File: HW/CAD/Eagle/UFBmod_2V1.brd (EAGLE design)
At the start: 98.4 x 89.5 mm, 197 parts, among them T0551 MMBT2222, U0501 MIDAS_MCCOG21605B6W-FPTLWI, U0601 MAX5217, U0701 AT86RF215-ZU, U0711 ASVTX-13-D-26.000MHZ-I05-T, U0811 PE4259, U0821 RFX1010, U0881 B39871B3440U410, U0911 FT232HL, U1101 TPS53353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

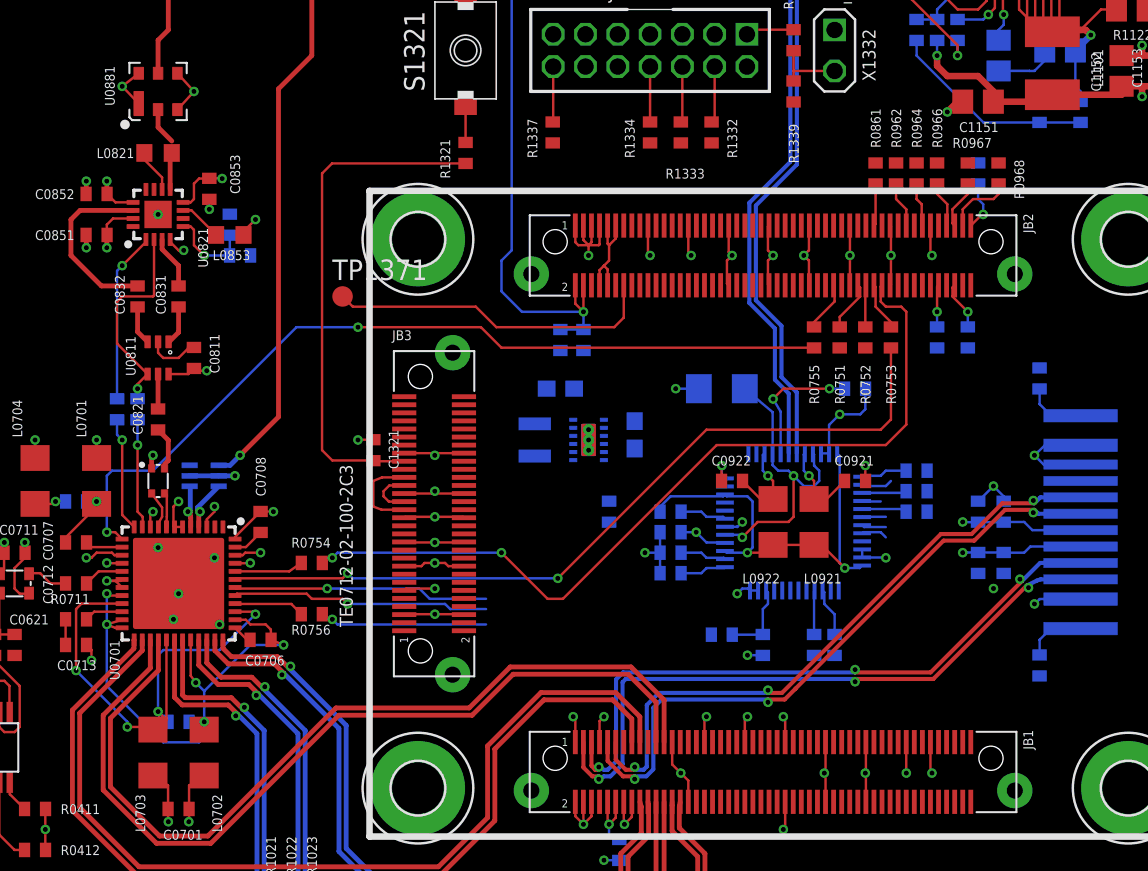
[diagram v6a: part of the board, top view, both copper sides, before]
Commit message: HW_2V0 - CAD/Eagle - some more wires routed
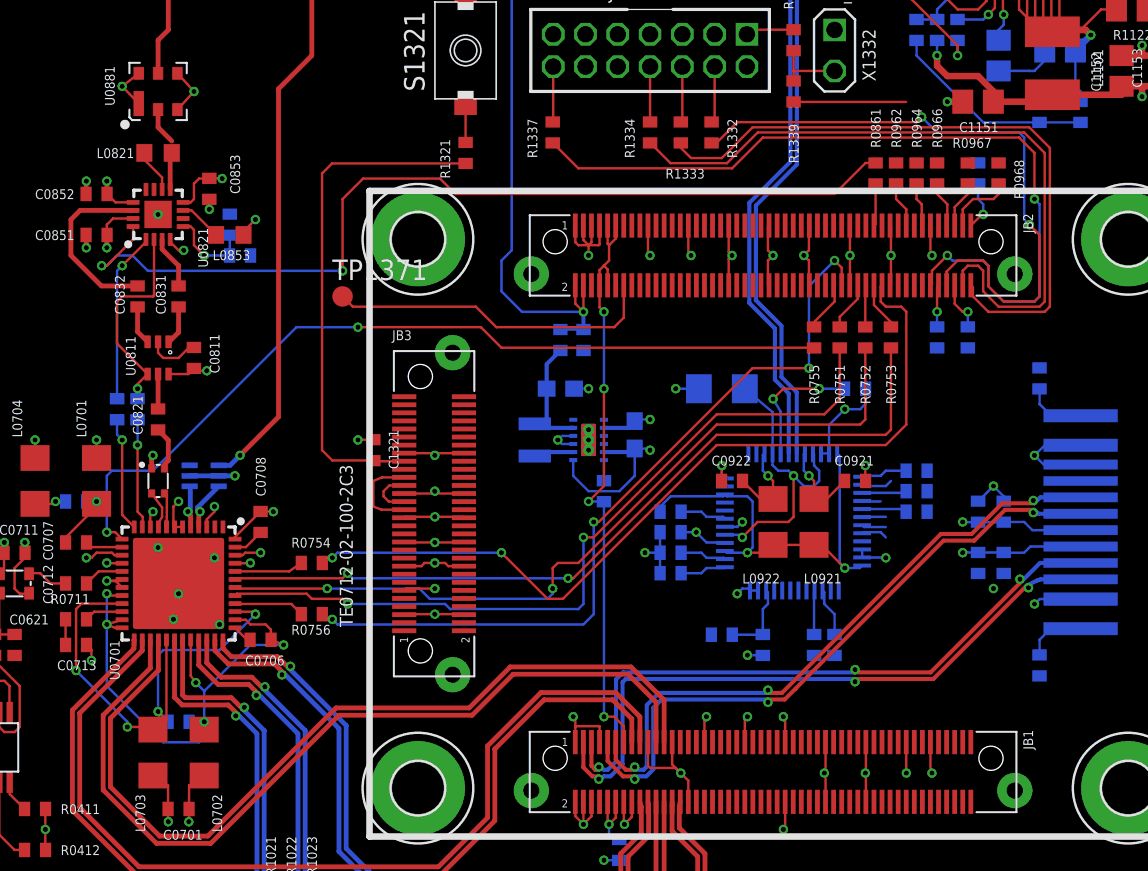
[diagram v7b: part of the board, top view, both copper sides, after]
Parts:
- moved R1211 1.31 mm to (45.4, 46.4)
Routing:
- net RFX_MODE: track 0.00 -> 58.2 mm, vias 0 -> 2
- net FPGA_SRST: track 0.00 -> 50.8 mm, vias 0 -> 2
- net FPGA_TDO: track 0.00 -> 43.5 mm
- net FPGA_TCK: track 0.00 -> 40.6 mm
- net FPGA_TMS: track 0.00 -> 39.6 mm, vias 0 -> 2
- net TRX_IRQ: track 10.4 -> 49.4 mm, vias 1 -> 4
- net TRX_SELN_R: track 15.8 -> 49.3 mm, vias 1 -> 2
- net TRX_SCLK_R: track 16.0 -> 48.9 mm, vias 1 -> 2
- net U3V3: track 6.68 -> 37.3 mm, vias 0 -> 4
- net +3V3: track 83.4 -> 95.2 mm, vias 20 -> 21
- net GND: track 227.7 -> 237.8 mm, vias 81 -> 83
- net +2V5: track 0.00 -> 8.26 mm
- net FPGA_JTAGEN: track 0.00 -> 6.97 mm
- net PMIC3V3_SW: track 0.00 -> 2.49 mm
- net TPS2_EN: track 0.00 -> 1.28 mm

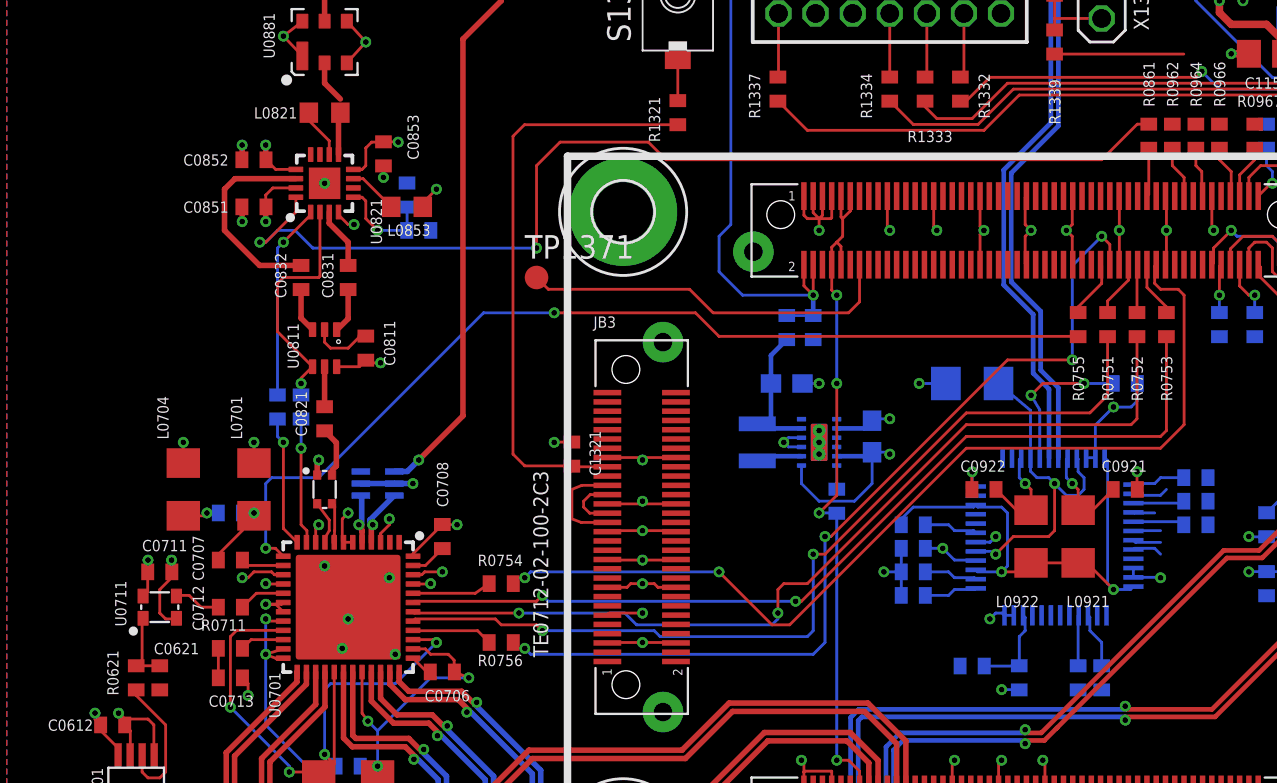
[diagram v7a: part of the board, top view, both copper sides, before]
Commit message: HW_2V0 - CAD/Eagle - more delicate signals routed
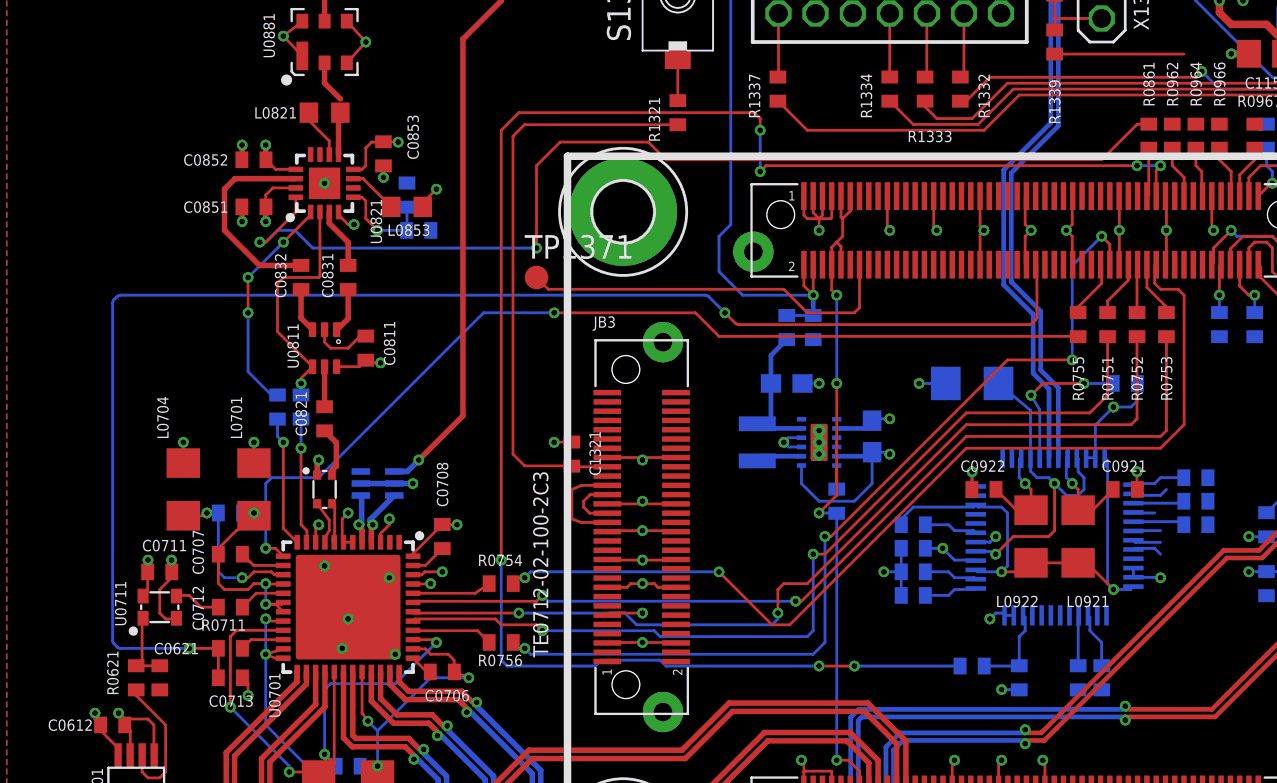
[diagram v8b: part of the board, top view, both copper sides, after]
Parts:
- moved C0707 0.32 mm to (12.7, 43.5)
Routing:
- net FPGA_FT_RESETN: track 0.00 -> 94.5 mm, vias 0 -> 7
- net TRX_CLK_26MHZ: track 1.59 -> 79.5 mm, vias 0 -> 2
- net TRX_AVSS: track 27.8 -> 33.0 mm
- net TRX_EVDD: track 6.01 -> 10.6 mm
- net RFX_RXEN: track 10.6 -> 12.6 mm, vias 1 -> 3
